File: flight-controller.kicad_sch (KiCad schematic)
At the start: 28 parts, among them J1 XT60PW-M, J2 Conn_01x04, J3 XT60PW-F, J4 XT60PW-F, J5 XT60PW-F, J6 XT60PW-F, U1 ACS773LCB-100B-PFF, U2 LMR33630ADDA, U3 AMS1117-3.3

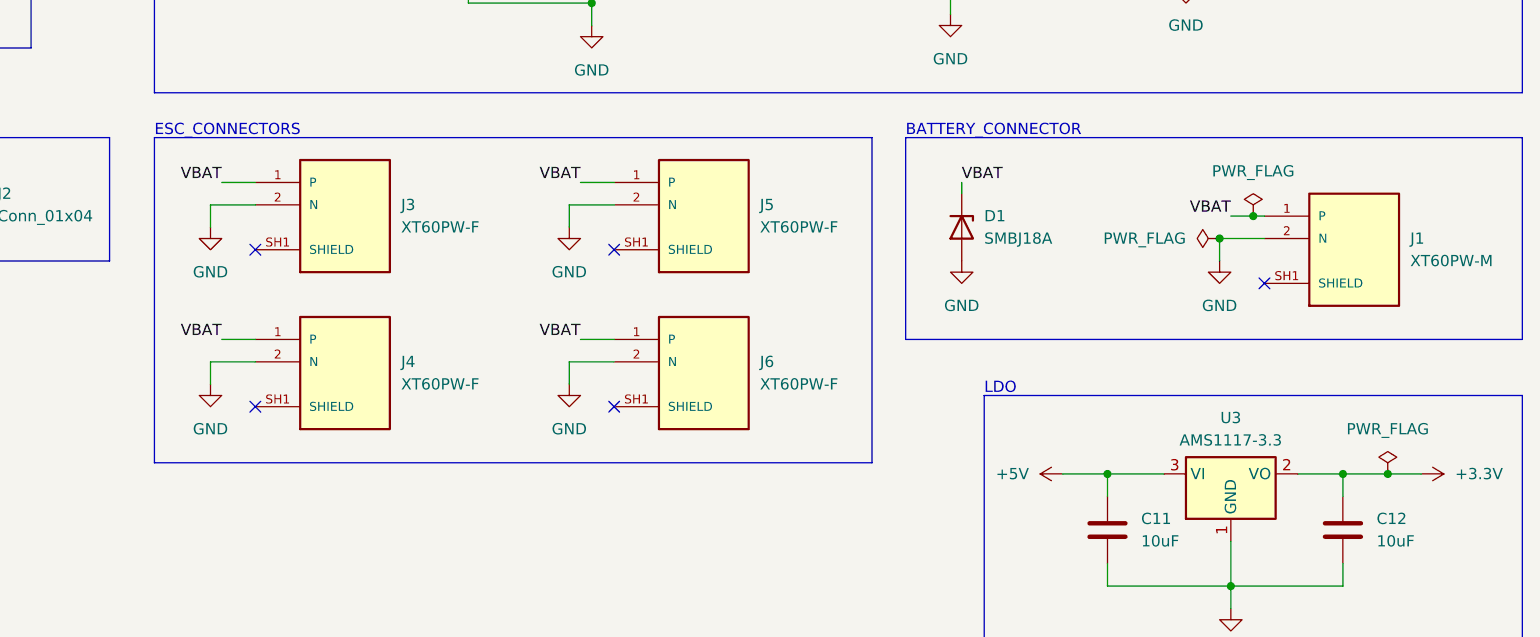
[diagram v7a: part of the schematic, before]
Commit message: fix: Fixed correct power input to XT60
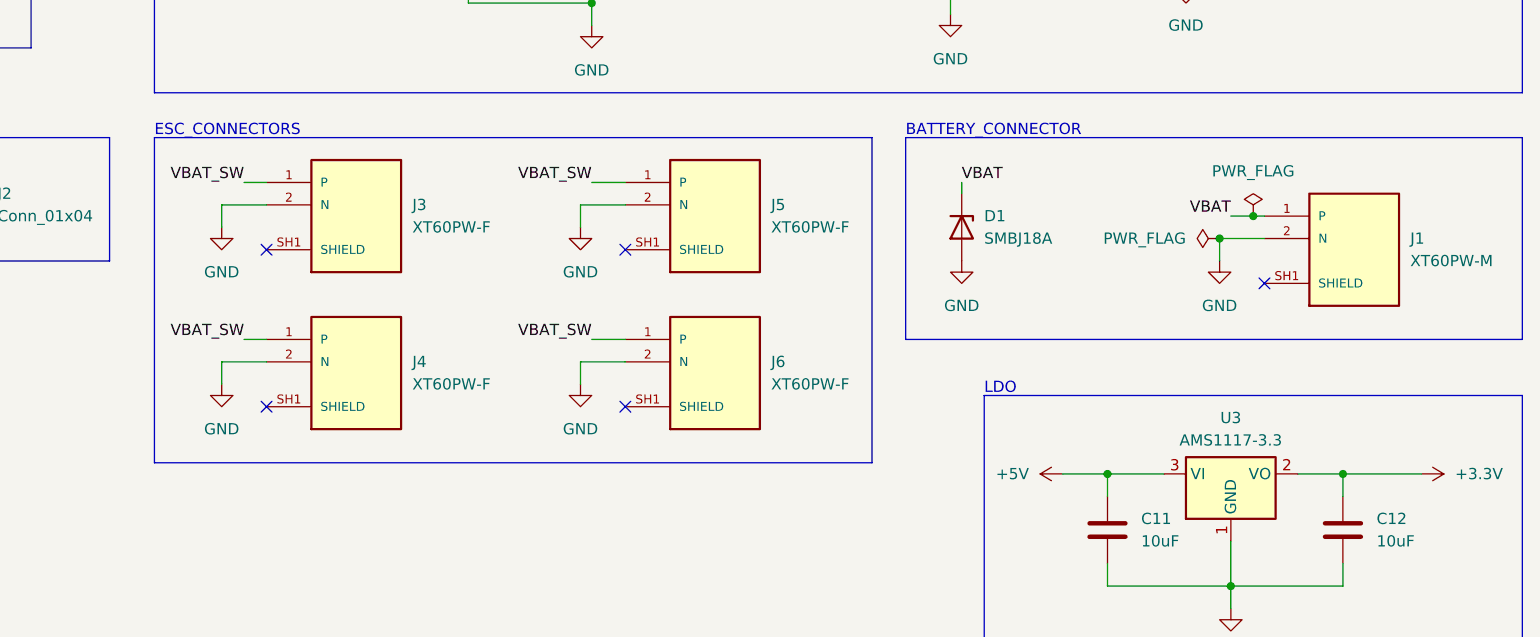
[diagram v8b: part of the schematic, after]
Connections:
- net VBAT: no longer J3.1 (P), J4.1 (P), J5.1 (P), J6.1 (P)
- net VBAT_SW: now also J3.1 (P), J4.1 (P), J5.1 (P), J6.1 (P)
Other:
- moved on the sheet: J3, J4, J5, J6
